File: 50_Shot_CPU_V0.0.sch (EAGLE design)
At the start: 74 parts, among them IC1 PIC24FJ128GA010, J1 J12, J10 22-23-2021, J11 22-23-2061, J12 A311422_nd, J13 22-23-2021, J14 22-23-2021, J3 22-23-2021, J4 22-23-2021, J5 22-23-2021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

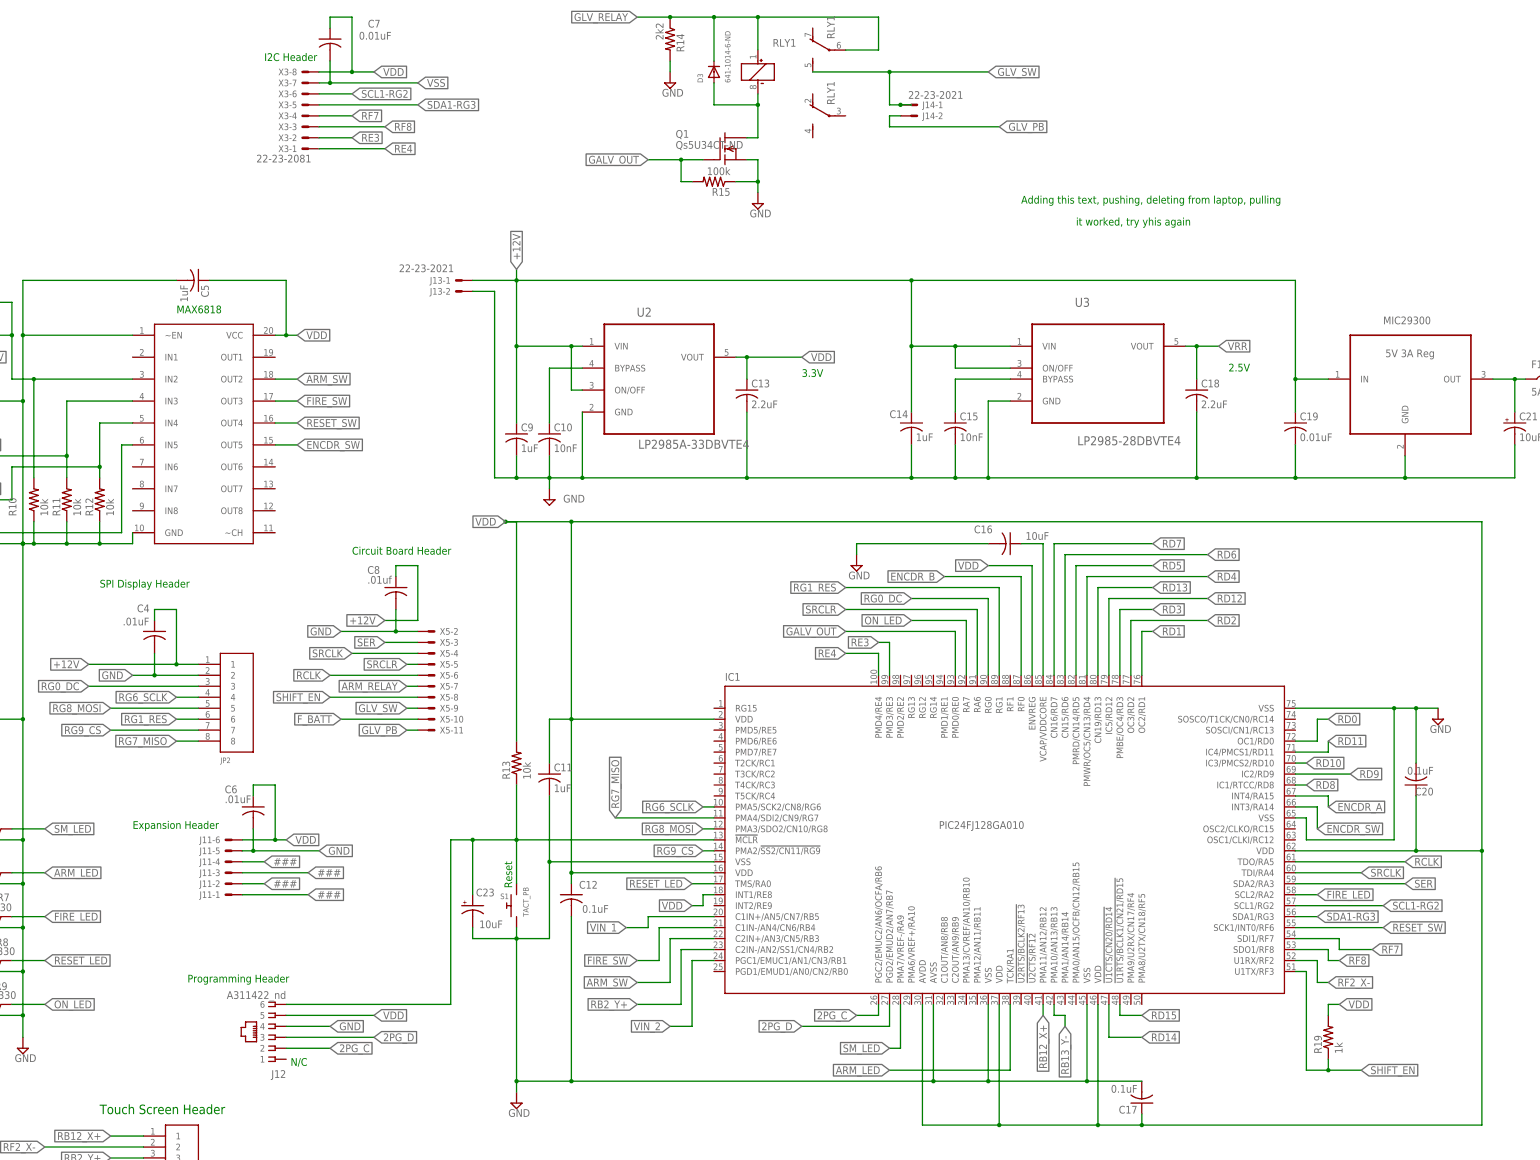
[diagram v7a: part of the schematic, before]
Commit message: converted programming header
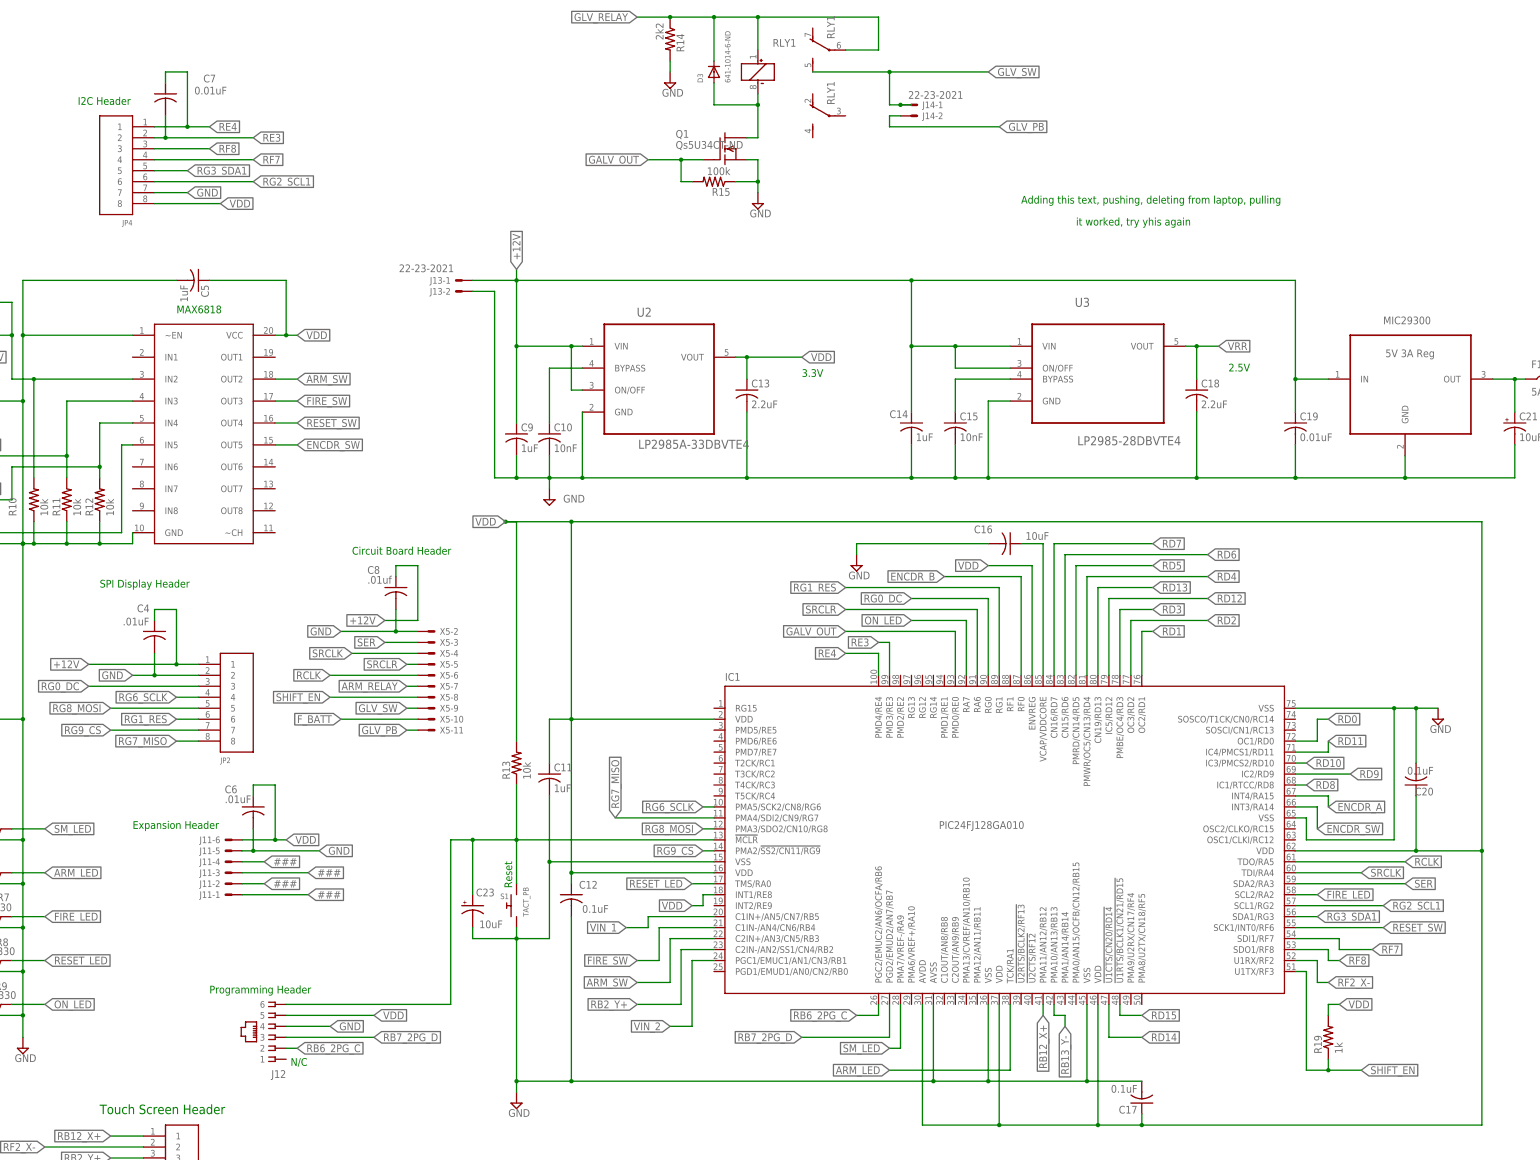
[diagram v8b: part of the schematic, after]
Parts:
- removed X3: 22-23-2081, con-molex:22-23-2081
- added JP4: SHERLOCK_8PIN_RGT, Mine:SHERLOCK_8PIN_RGT
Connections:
- net 2PG_C renamed RB6_2PG_C
- net 2PG_D renamed RB7_2PG_D
- removed net SCL1-RG2: IC1.SCL1/RG2, X3-6.S
- removed net SDA1-RG3: IC1.SDA1/RG3, X3-5.S
- removed net VSS: C7.2, X3-7.S
- new net RG2_SCL1: IC1.SCL1/RG2, JP4.6
- new net RG3_SDA1: IC1.SDA1/RG3, JP4.5
- net GND: now also JP4.7
- net RE3: now also C7.2, JP4.2; no longer X3-2.S
- net RE4: now also C7.1, JP4.1; no longer X3-1.S
- net RF7: now also JP4.4; no longer X3-4.S
- net RF8: now also JP4.3; no longer X3-3.S
- net VDD: now also JP4.8; no longer C7.1, X3-8.S
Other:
- moved on the sheet: C7
